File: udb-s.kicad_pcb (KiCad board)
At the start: 4 copper layers, 40 x 9 mm, 11 parts, among them J1 TYPE-C-31-M-12, J2 78171-0004, U1 TPD4E05U06DQAR

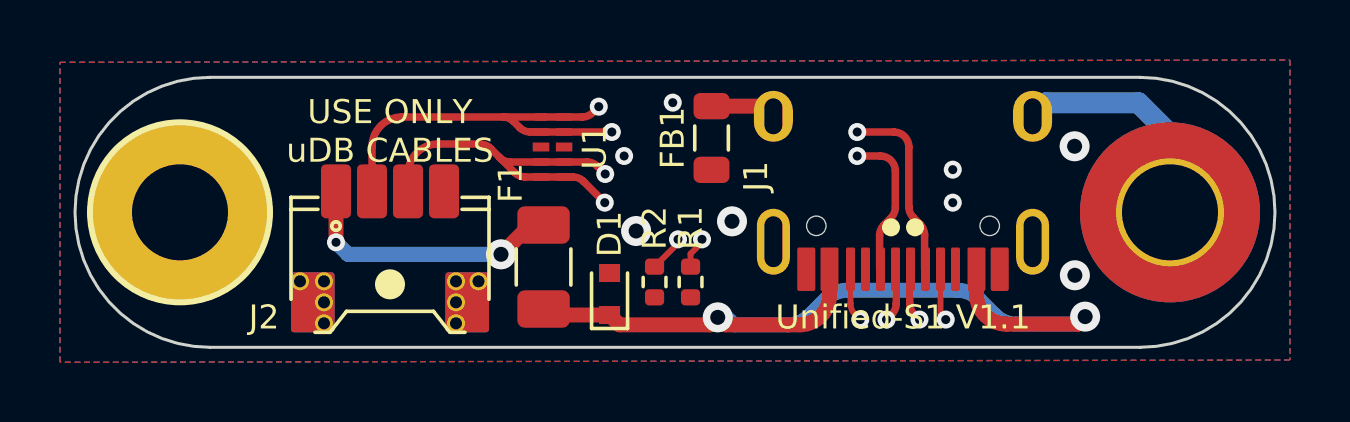
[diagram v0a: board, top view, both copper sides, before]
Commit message: Update grounding, remove FB1, new prod files
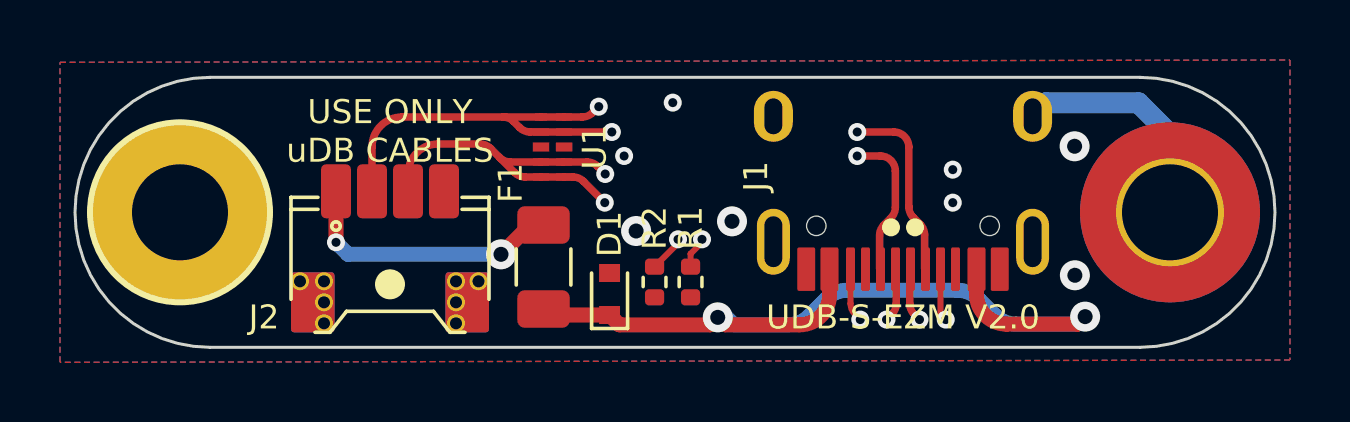
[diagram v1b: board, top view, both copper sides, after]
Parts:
- removed FB1: GZ2012D601TF, Inductor_SMD:L_0805_2012Metric
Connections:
- H1 pad 1: GNDPWR -> GND
- J1 pad S1: GNDPWR -> GND
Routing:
- net GNDPWR: track 10.0 -> 0.00 mm
- net GND: track 0.43 -> 8.23 mm
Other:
- board text added: "UDB-S-EZM V2.0"
- board text added: "UDB-S-EZM V2.0 www.unified- daughterboard.github.io"
- board text removed: "Unified-S1 V1.1"
- board text removed: "Unified-S1 V1.1 www.unified- daughterboard.github.io"

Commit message: Update submodules, change EZM for JST
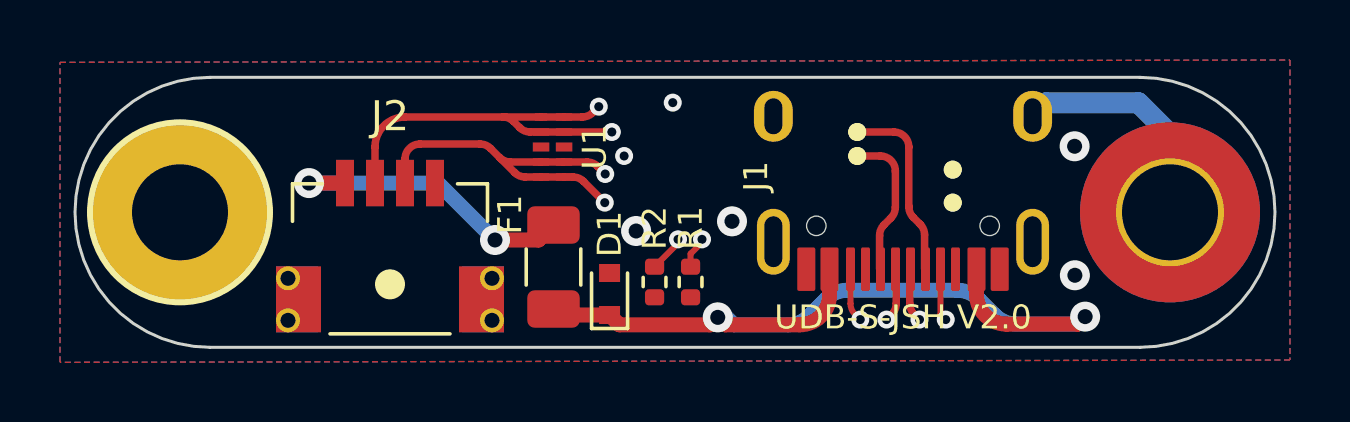
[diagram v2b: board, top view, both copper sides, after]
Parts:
- J2: value 78171-0004 -> A1001WR-S-04P; footprint locallib:PicoEZMate-Reinforced-Lite -> acheron_Connectors:SM04B-SRSS-TB(LF)(SN)_mounting-reliefs
- moved J2 1.70 mm to (122.0, 94.8)
- moved F1 0.33 mm to (127.5, 96.8)
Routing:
- net 5V: track 9.19 -> 10.3 mm
- net D+: track 49.6 -> 50.2 mm
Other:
- board text added: "UDB-S-JSH V2.0"
- board text added: "UDB-S-JSH V2.0 www.unified- daughterboard.github.io"
- board text removed: "UDB-S-EZM V2.0"
- board text removed: "UDB-S-EZM V2.0 www.unified- daughterboard.github.io"
- board text removed: "USE ONLY uDB CABLES"
